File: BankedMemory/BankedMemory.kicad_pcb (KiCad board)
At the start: 2 copper layers, 100 x 100 mm, 24 parts, among them J1 Buss, U1 AS6C4008_{0}, U2 AS6C4008_{1}, U3 74LS00, U4 GAL22V10, U5 74LS573, U6 DS1210, U7 DS1210

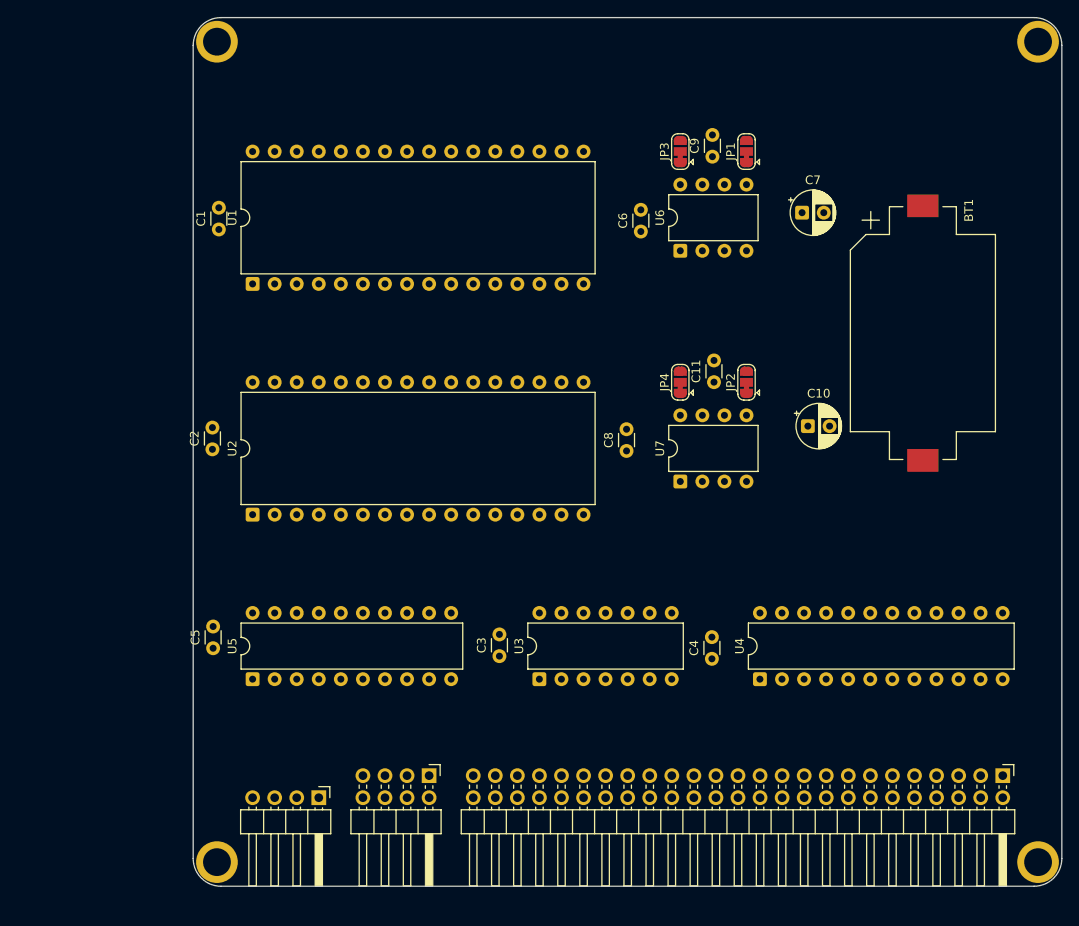
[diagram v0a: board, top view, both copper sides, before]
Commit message: finish routing the coms board. add some step models to look at this thing in freecad
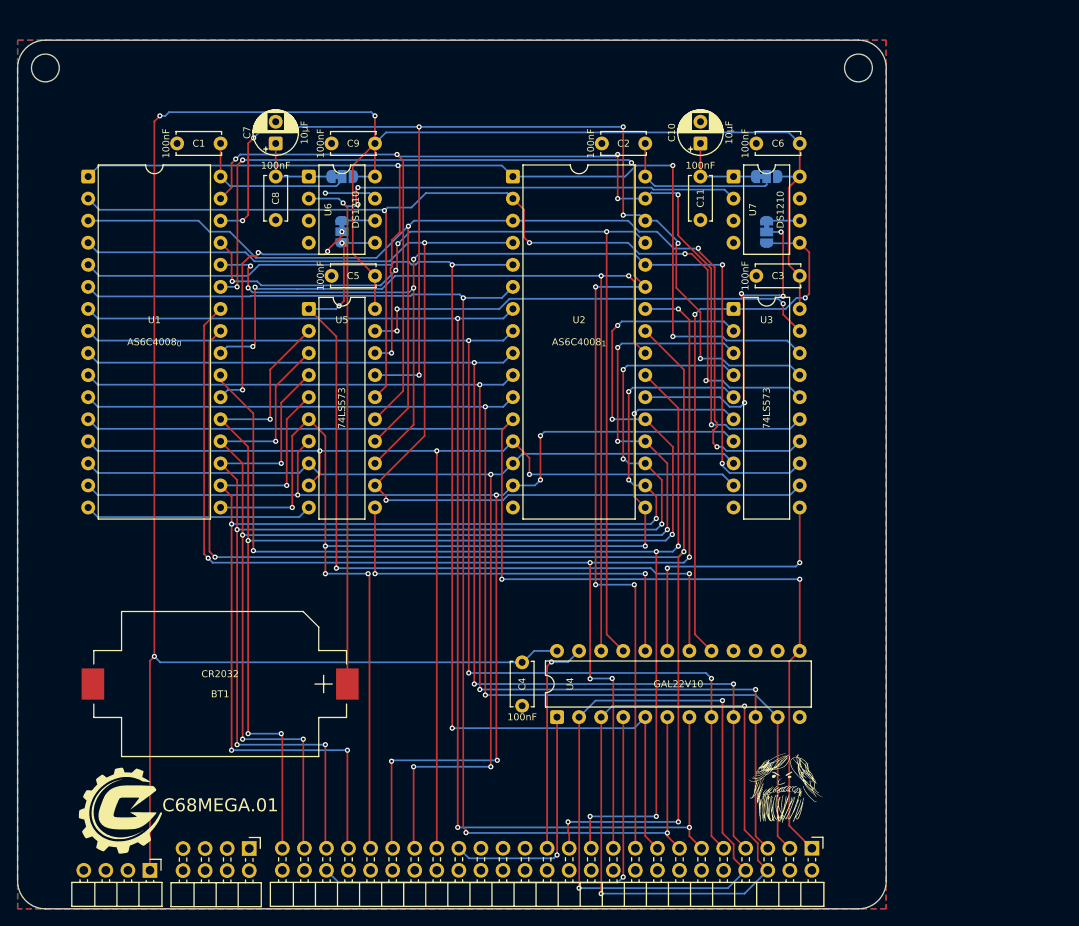
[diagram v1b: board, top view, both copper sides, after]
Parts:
- added G1: Logo, 0-Footprints:Crank, F.Cu at (36.9, 113.7)
- added G2: Logo, 0-Footprints:crankery_small, F.Cu at (113.1, 111.2)
- BT1: footprint Battery:BatteryHolder_Keystone_1060_1x2032 -> 0-Footprints:BatteryHolder_Keystone_1060_1x2032
- C1, C11, C2, C3, C4, C5, C6, C8, C9: value 100n -> 100nF; footprint Capacitor_THT:C_Disc_D3.0mm_W1.6mm_P2.50mm -> 0-Footprints:C_Disc_D5.0mm_W2.5mm_P5.00mm
- C10, C7: footprint Capacitor_THT:CP_Radial_D5.0mm_P2.50mm -> 0-Footprints:CP_Radial_D5.0mm_P2.50mm
- J1: value Buss -> Card
- JP1, JP3: value BE -> Low; moved to B.Cu
- JP2, JP4: value BE -> High; moved to B.Cu
- U1, U2: footprint Package_DIP:DIP-32_W15.24mm -> 0-Footprints:DIP-32_W15.24mm
- U3: value 74LS00 -> 74LS573; footprint Package_DIP:DIP-14_W7.62mm -> 0-Footprints:DIP-20_W7.62mm
- U4: footprint Package_DIP:DIP-24_W7.62mm -> 0-Footprints:DIP-24_W7.62mm
- U5: footprint Package_DIP:DIP-20_W7.62mm -> 0-Footprints:DIP-20_W7.62mm
- U6, U7: footprint Package_DIP:DIP-8_W7.62mm -> 0-Footprints:DIP-8_W7.62mm
- moved BT1 90.4 mm to (48.3, 99.1), turned to 180 degrees
- moved C7 61.1 mm to (54.7, 36.9), turned to 90 degrees
- moved C2 61.0 mm to (97.3, 36.9), turned to 180 degrees
- moved C3 55.8 mm to (115.0, 52.1), turned to 180 degrees
- moved U2 49.1 mm to (82.0, 40.7), turned to 0 degrees
- moved C8 48.4 mm to (54.7, 45.7)
- moved U3 48.1 mm to (107.4, 55.9), turned to 0 degrees
- moved C5 46.7 mm to (66.1, 52.1), turned to 180 degrees
- moved JP1 46.6 mm to (62.4, 40.7), turned to 0 degrees
- moved U6 43.6 mm to (58.5, 40.7), turned to 0 degrees
- moved U5 43.1 mm to (58.5, 55.9), turned to 0 degrees
- moved JP3 40.0 mm to (62.3, 47.0), turned to -90 degrees
- moved C9 38.9 mm to (66.1, 36.9), turned to 180 degrees
- moved U7 35.6 mm to (107.4, 40.7), turned to 0 degrees
- moved C10 34.8 mm to (103.6, 36.9), turned to 90 degrees
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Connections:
- net +5V_{B1} renamed +5V_{LB}
- net +5V_{B2} renamed +5V_{HB}
- C5 pad 1: GND -> +5V
- C5 pad 2: +5V_{B} -> GND
- J1 pad 27: A13 -> unconnected-(J1-A_{13}-Pad27)
- J1 pad 29: A14 -> unconnected-(J1-A_{14}-Pad29)
- J1 pad 31: A15 -> unconnected-(J1-A_{15}-Pad31)
- JP3 pad 1: ~{BANK_SEL_{0}_B} -> ~{BANK_{LB}}
- JP3 pad 3: ~{BANK_SEL_{0}} -> ~{BANK_{L}}
- JP4 pad 1: ~{BANK_SEL_{1}_B} -> ~{BANK_{HB}}
- JP4 pad 3: ~{BANK_SEL_{1}} -> ~{BANK_{H}}
- U1 pad 1: BANK_5 -> BANK_6
- U1 pad 2: BANK_3 -> BANK_4
- U1 pad 28: BANK_0 -> BANK_1
- U1 pad 3: BANK_1 -> BANK_2
- U1 pad 30: BANK_4 -> BANK_5
- U1 pad 31: BANK_2 -> BANK_3
- U1 pad 4: A12 -> BANK_0
- U2 pad 1: BANK_5 -> BANK_6
- U2 pad 2: BANK_3 -> BANK_4
- U2 pad 28: BANK_0 -> BANK_1
- U2 pad 3: BANK_1 -> BANK_2
- U2 pad 30: BANK_4 -> BANK_5
- U2 pad 31: BANK_2 -> BANK_3
- U2 pad 4: A12 -> BANK_0
- U3 pad 1: BANK6 -> ~{BANK_{H}}
- U3 pad 10: ~{BANK6} -> GND
- U3 pad 11: unconnected-(U3-Pad11) -> LOAD_{H}
- U3 pad 12: GND -> BANK_0
- U3 pad 13: GND -> BANK_1
- U3 pad 14: +5V_{B} -> BANK_2
- U3 pad 2: BANK6 -> D7
- U3 pad 3: ~{BANK6} -> D6
- U3 pad 4: ~{BANK_SEL_B} -> D5
- U3 pad 5: BANK6 -> D4
- U3 pad 6: ~{BANK_CS_{0}} -> D3
- U3 pad 7: GND -> D2
- U3 pad 8: ~{BANK_CS_{1}} -> D1
- U3 pad 9: ~{BANK_SEL_B} -> D0
- U4 pad 17: GND -> ~{BANK_{H}}
- U4 pad 18: GND -> ~{BANK_{L}}
- U4 pad 19: GND -> LOAD_{H}
- U4 pad 20: GND -> LOAD_{L}
- U4 pad 21: LOAD_LATCH -> ~{WE}
- U4 pad 22: ~{WE} -> ~{OE}
- U4 pad 23: ~{OE} -> A12
- U5 pad 1: GND -> ~{BANK_{L}}
- U5 pad 11: LOAD_LATCH -> LOAD_{L}
- U6 pad 5: ~{BANK_CS_{0}} -> ~{BANK_{L}}
- U6 pad 6: ~{BANK_CS_{0}_B} -> ~{BANK_{LB}}
- U7 pad 5: ~{BANK_CS_{1}} -> ~{BANK_{H}}
- U7 pad 6: ~{BANK_CS_{1}_B} -> ~{BANK_{HB}}
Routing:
- net +5V: track 0.00 -> 262.8 mm, vias 0 -> 3
- net D7: track 0.00 -> 164.9 mm, vias 0 -> 7
- net D6: track 0.00 -> 161.2 mm, vias 0 -> 7
- net D5: track 0.00 -> 156.9 mm, vias 0 -> 7
- net A11: track 0.00 -> 155.5 mm, vias 0 -> 4
- net A9: track 0.00 -> 154.0 mm, vias 0 -> 6
- net D4: track 0.00 -> 152.9 mm, vias 0 -> 7
- net A8: track 0.00 -> 151.5 mm, vias 0 -> 6
- net A5: track 0.00 -> 150.7 mm, vias 0 -> 3
- net A6: track 0.00 -> 150.7 mm, vias 0 -> 3
- net A7: track 0.00 -> 142.3 mm, vias 0 -> 2
- net D2: track 0.00 -> 140.6 mm, vias 0 -> 6
- net D3: track 0.00 -> 138.9 mm, vias 0 -> 6
- net A4: track 0.00 -> 136.4 mm, vias 0 -> 3
- net A3: track 0.00 -> 136.1 mm, vias 0 -> 3
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- added copper zone on B.Cu, net GND
- added copper zone on F.Cu, net GND
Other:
- board text added: "C68MEGA.01"
- board text added: "Crankery - April 2026 - Dave Hamilton"

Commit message: lots of fixes to stack handling on emu, fix the latches on the banked memory board, tons of little bug fixes
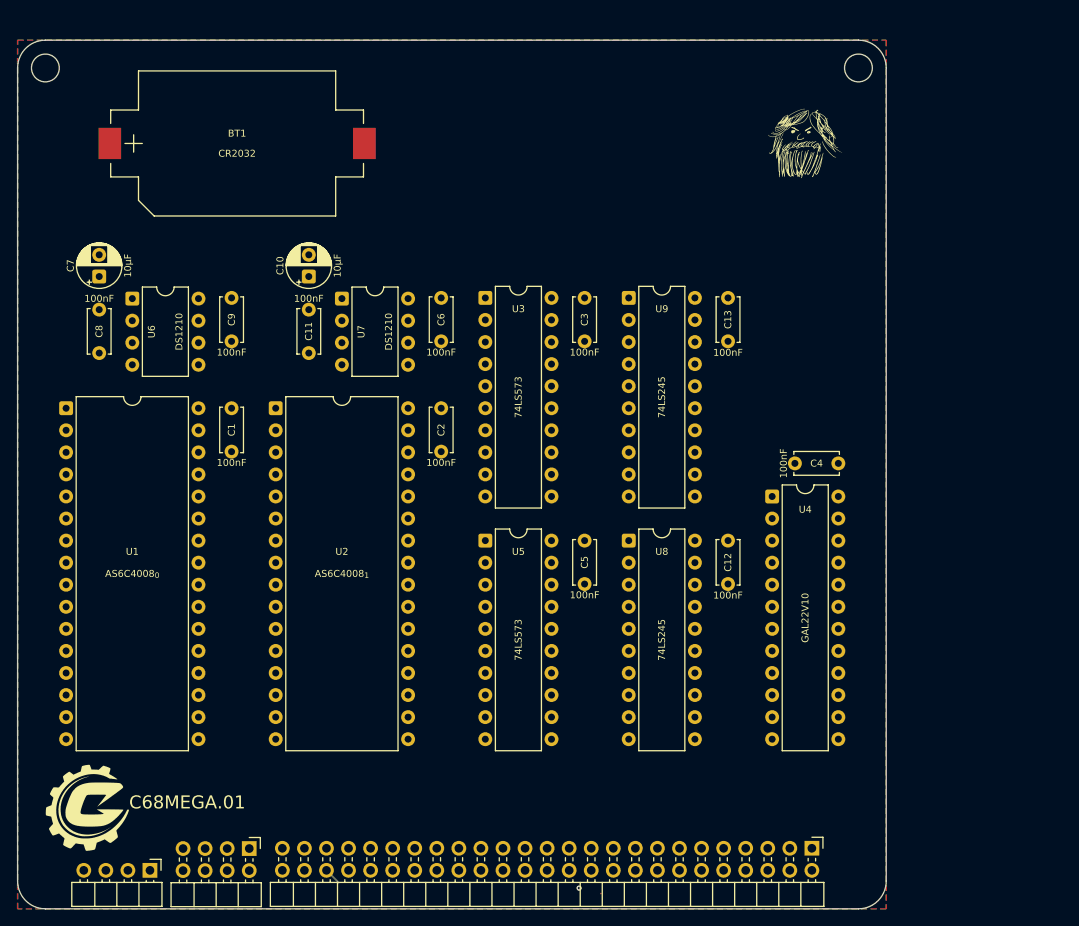
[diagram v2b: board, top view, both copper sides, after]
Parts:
- removed JP1, JP3: Low, Jumper:SolderJumper-3_P1.3mm_Bridged12_RoundedPad1.0x1.5mm
- removed JP2, JP4: High, Jumper:SolderJumper-3_P1.3mm_Bridged12_RoundedPad1.0x1.5mm
- added C12: 100nF, 0-Footprints:C_Disc_D5.0mm_W2.5mm_P5.00mm, F.Cu at (106.8, 82.6)
- added C13: 100nF, 0-Footprints:C_Disc_D5.0mm_W2.5mm_P5.00mm, F.Cu at (106.8, 54.7)
- added U8: 74LS245, 0-Footprints:DIP-20_W7.62mm, F.Cu at (95.4, 82.6)
- added U9: 74LS245, 0-Footprints:DIP-20_W7.62mm, F.Cu at (95.4, 54.7)
- moved G2 74.2 mm to (115.3, 37.0)
- moved BT1 62.3 mm to (50.3, 36.9), turned to 0 degrees
- moved C10 47.6 mm to (58.5, 52.2)
- moved C11 47.6 mm to (58.5, 61.0)
- moved U7 47.2 mm to (62.3, 54.8)
- moved C6 44.9 mm to (73.8, 54.7), turned to -90 degrees
- moved C4 43.0 mm to (119.5, 73.7), turned to 180 degrees
- moved C5 38.9 mm to (90.3, 82.6), turned to -90 degrees
- moved C2 38.5 mm to (73.8, 67.4), turned to -90 degrees
- moved U2 38.2 mm to (54.7, 67.4)
- moved U4 35.5 mm to (111.9, 77.5), turned to 0 degrees
- moved U5 33.5 mm to (78.8, 82.6)
- moved C1 30.5 mm to (49.6, 67.4), turned to -90 degrees
- moved U3 28.6 mm to (78.8, 54.7)
- moved U1 26.8 mm to (30.6, 67.4)
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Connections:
- C1 pad 1: Net-(JP1-C) -> +5V_{LB}
- C2 pad 1: Net-(JP2-C) -> +5V_{HB}
- U1 pad 22: Net-(JP3-C) -> ~{CS_RAM_{LB}}
- U1 pad 32: Net-(JP1-C) -> +5V_{LB}
- U2 pad 22: Net-(JP4-C) -> ~{CS_RAM_{HB}}
- U2 pad 32: Net-(JP2-C) -> +5V_{HB}
- U3 pad 1: ~{BANK_{H}} -> GND
- U3 pad 12: BANK_0 -> LATCH_BANK7_H
- U3 pad 13: BANK_1 -> Net-(U3-Q6)
- U3 pad 14: BANK_2 -> Net-(U3-Q5)
- U3 pad 15: BANK_3 -> Net-(U3-Q4)
- U3 pad 16: BANK_4 -> Net-(U3-Q3)
- U3 pad 17: BANK_5 -> Net-(U3-Q2)
- U3 pad 18: BANK_6 -> Net-(U3-Q1)
- U3 pad 19: BANK_7 -> Net-(U3-Q0)
- U3 pad 2: D7 -> D0
- U3 pad 3: D6 -> D1
- U3 pad 4: D5 -> D2
- U3 pad 5: D4 -> D3
- U3 pad 6: D3 -> D4
- U3 pad 7: D2 -> D5
- U3 pad 8: D1 -> D6
- U3 pad 9: D0 -> D7
- U4 pad 15: GND -> LOAD_{H}
- U4 pad 16: GND -> LOAD_{L}
- U4 pad 17: ~{BANK_{H}} -> ~{WE}
- U4 pad 18: ~{BANK_{L}} -> ~{OE}
- U4 pad 19: LOAD_{H} -> ~{CS_RAM_{H}}
- U4 pad 20: LOAD_{L} -> ~{CS_RAM_{L}}
- U4 pad 21: ~{WE} -> LATCH_BANK7_H
- U4 pad 22: ~{OE} -> LATCH_BANK7_L
- U5 pad 1: ~{BANK_{L}} -> GND
- U5 pad 12: BANK_0 -> LATCH_BANK7_L
- U5 pad 13: BANK_1 -> Net-(U5-Q6)
- U5 pad 14: BANK_2 -> Net-(U5-Q5)
- U5 pad 15: BANK_3 -> Net-(U5-Q4)
- U5 pad 16: BANK_4 -> Net-(U5-Q3)
- U5 pad 17: BANK_5 -> Net-(U5-Q2)
- U5 pad 18: BANK_6 -> Net-(U5-Q1)
- U5 pad 19: BANK_7 -> Net-(U5-Q0)
- U5 pad 2: D7 -> D0
- U5 pad 3: D6 -> D1
- U5 pad 4: D5 -> D2
- U5 pad 5: D4 -> D3
- U5 pad 6: D3 -> D4
- U5 pad 7: D2 -> D5
- U5 pad 8: D1 -> D6
- U5 pad 9: D0 -> D7
- U6 pad 5: ~{BANK_{L}} -> ~{CS_RAM_{L}}
- U6 pad 6: ~{BANK_{LB}} -> ~{CS_RAM_{LB}}
- U7 pad 5: ~{BANK_{H}} -> ~{CS_RAM_{H}}
- U7 pad 6: ~{BANK_{HB}} -> ~{CS_RAM_{HB}}
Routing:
- net +5V: track 262.8 -> 0.00 mm, vias 3 -> 0
- net D7: track 164.9 -> 0.00 mm, vias 7 -> 0
- net D6: track 161.2 -> 0.00 mm, vias 7 -> 0
- net D5: track 156.9 -> 0.00 mm, vias 7 -> 0
- net A11: track 155.5 -> 0.00 mm, vias 4 -> 0
- net A9: track 154.0 -> 0.00 mm, vias 6 -> 0
- net D4: track 152.9 -> 0.00 mm, vias 7 -> 0
- net A8: track 151.5 -> 0.00 mm, vias 6 -> 0
- net A5: track 150.7 -> 0.00 mm, vias 3 -> 0
- net A6: track 150.7 -> 0.00 mm, vias 3 -> 0
- net A7: track 142.3 -> 0.00 mm, vias 2 -> 0
- net D2: track 140.6 -> 0.00 mm, vias 6 -> 0
- net D3: track 138.9 -> 0.00 mm, vias 6 -> 0
- net A4: track 136.4 -> 0.00 mm, vias 3 -> 0
- net A3: track 136.1 -> 0.00 mm, vias 3 -> 0
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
